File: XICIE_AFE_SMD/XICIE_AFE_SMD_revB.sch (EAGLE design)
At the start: 45 parts, among them IC1 LM324D, IC2 CY8C4245T, IC3 AAT1217, J1 22-27-2021-02, Q1 MOSFET-NCHANNELBSS123LT1G, Q2 MOSFET-NCHANNELBSS123LT1G, Q3 MOSFET-NCHANNELBSS123LT1G

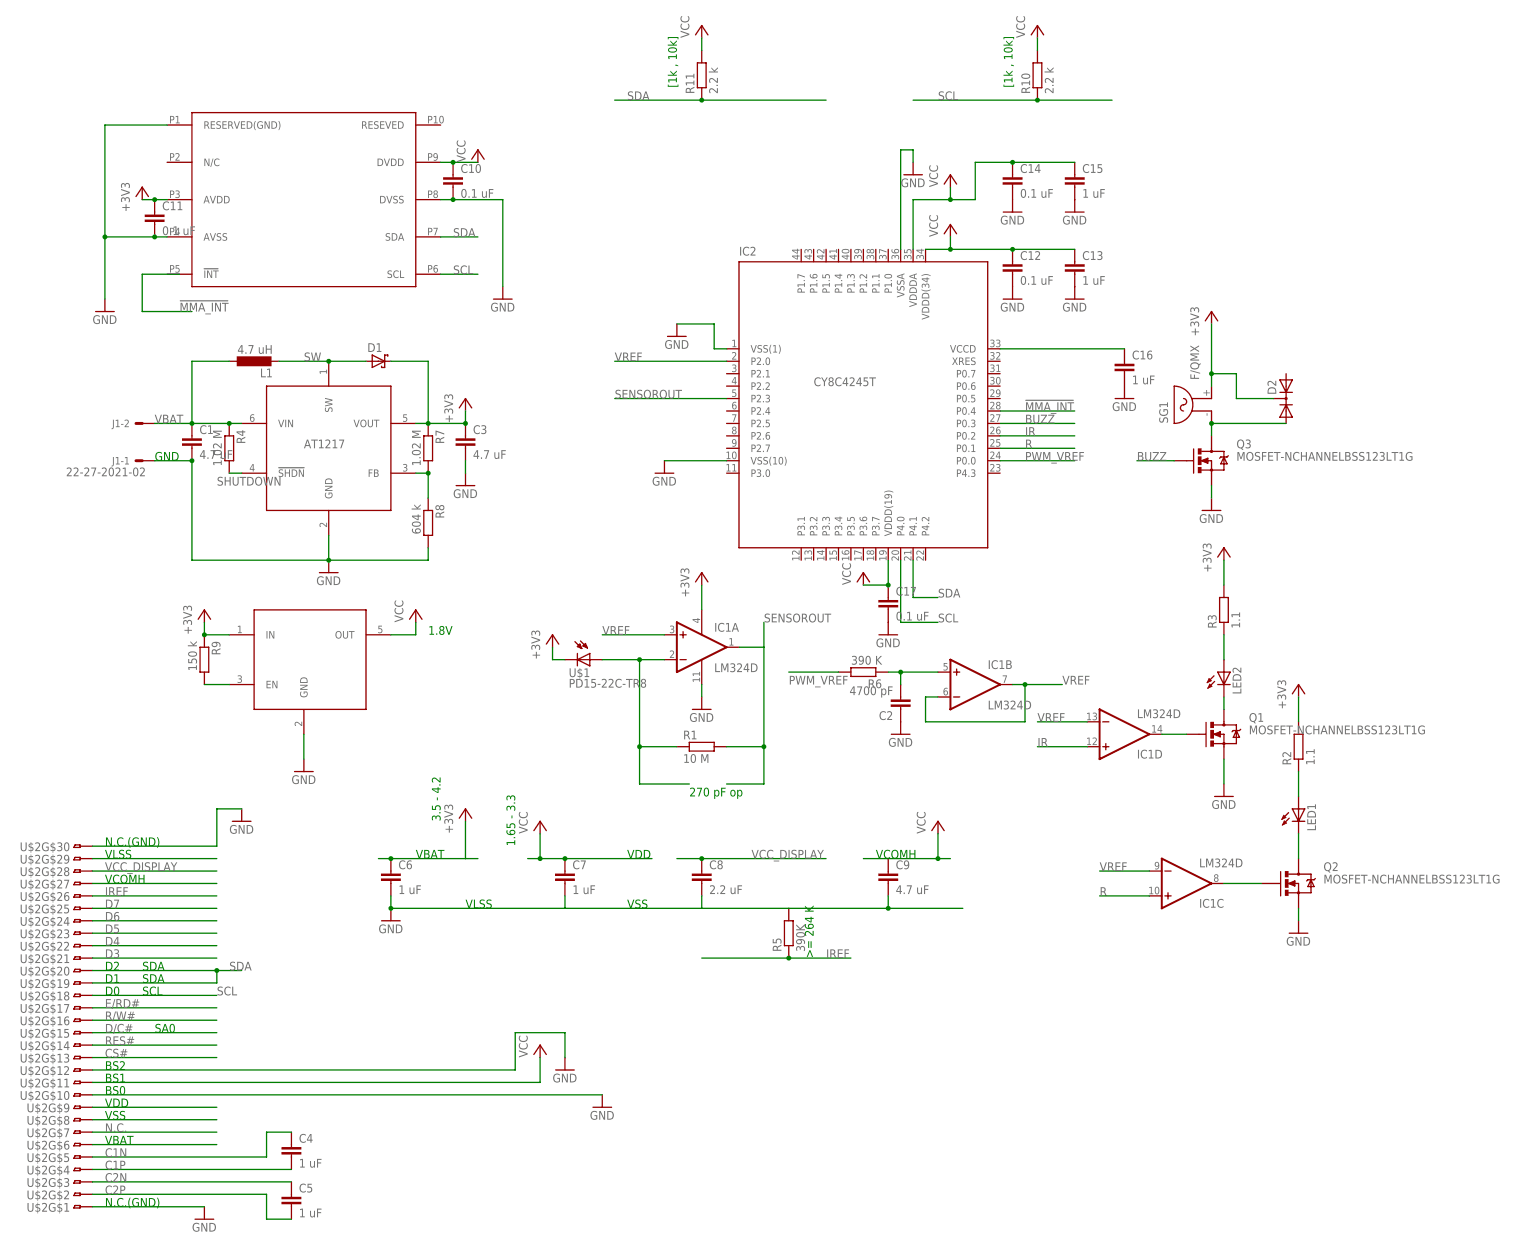
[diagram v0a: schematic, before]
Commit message: Finished rev B of XICIE_AFE_SMD
Many things added, like button, buzzer, RGB
led. Placing improved manually. Still missing
connection to program PSoC4.
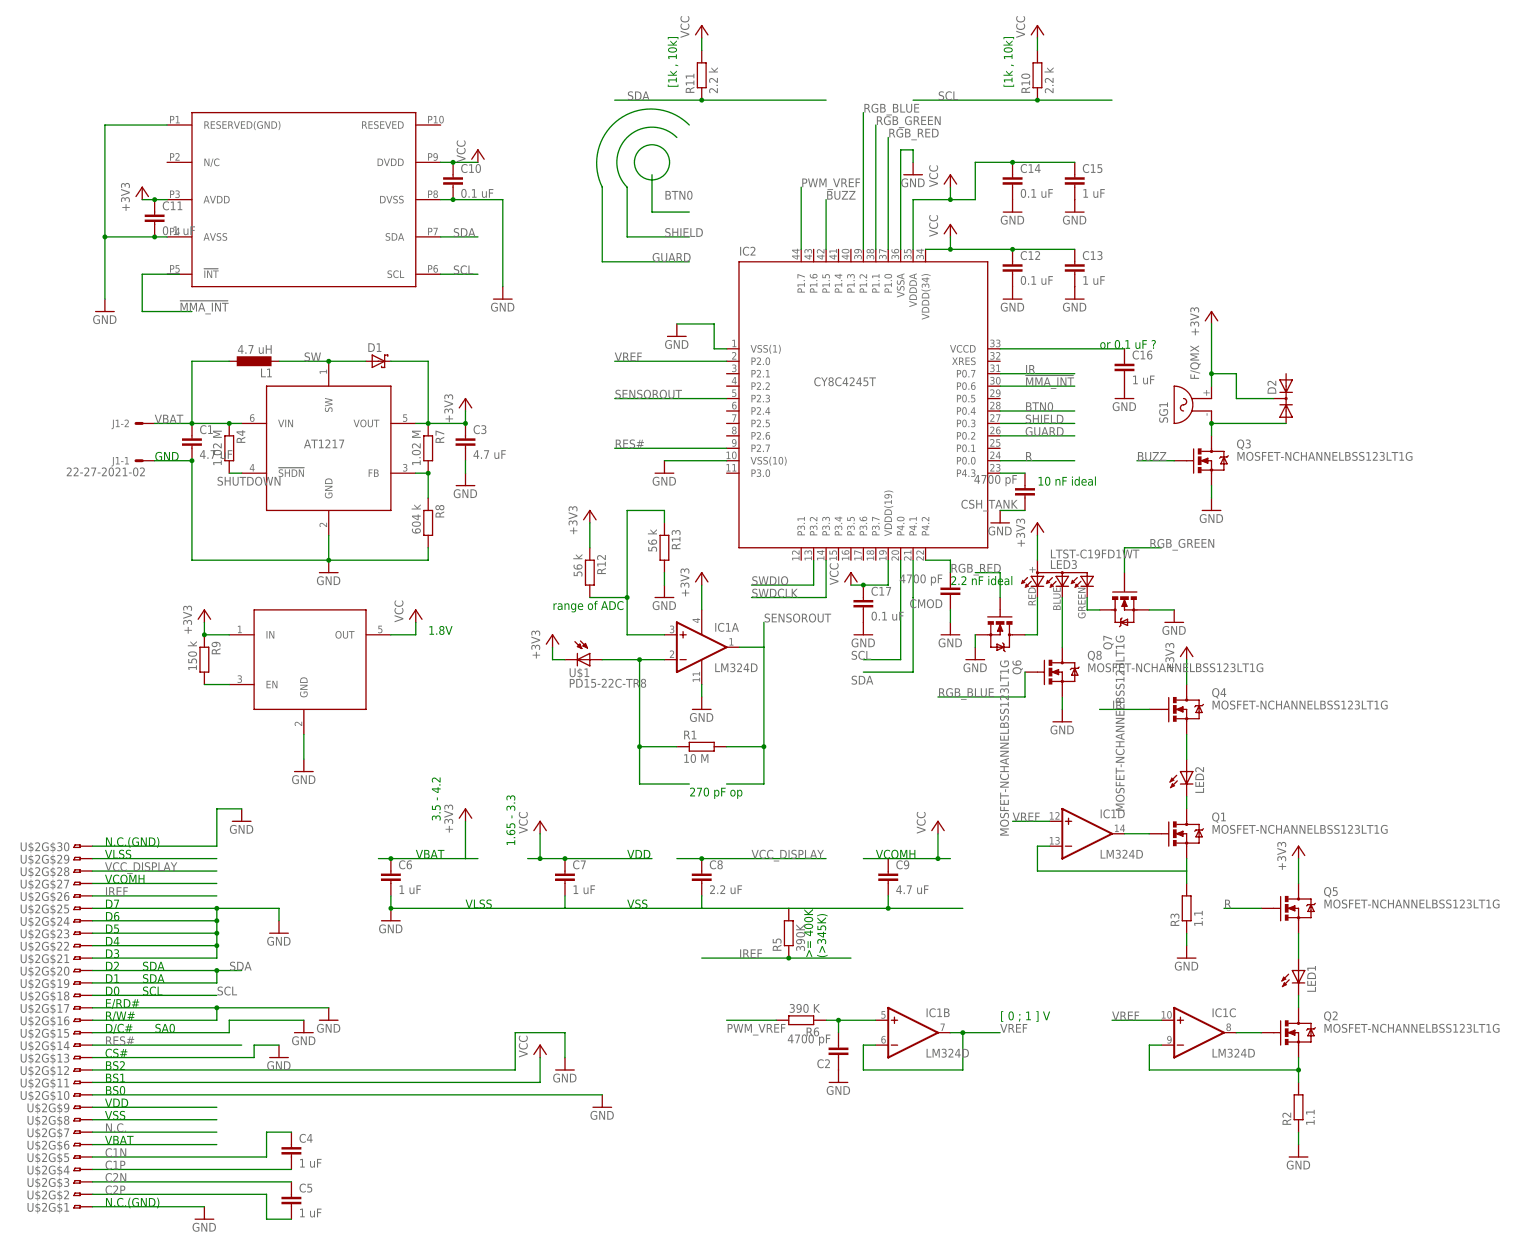
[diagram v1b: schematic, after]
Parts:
- added CMOD, CSH_TANK: 4700 pF, rcl:C-EUC0402
- added LED3: LTST-C19FD1WT, juliano:LTST-C19FD1WT
- added Q4, Q5, Q6, Q7, Q8: MOSFET-NCHANNELBSS123LT1G, SparkFun-DiscreteSemi:MOSFET-NCHANNELBSS123LT1G
- added R12, R13: 56 k, rcl:R-EU_R0603
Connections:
- removed net CS#: U$2G$13.1
- removed net D/C#: U$2G$15.1
- removed net D3: U$2G$21.1
- removed net D4: U$2G$22.1
- removed net D5: U$2G$23.1
- removed net D6: U$2G$24.1
- removed net D7: U$2G$25.1
- removed net E/RD#: U$2G$17.1
- removed net N$7 (its old number): LED1.A, R2.1
- removed net R/W#: U$2G$16.1
- new net BTN0: IC2.P0.4
- new net GUARD: IC2.P0.2
- new net N$15: IC1A.+IN, R12.2, R13.1
- new net N$16: LED1.A, Q5.S
- new net N$17: LED3.CRED, Q6.D
- new net N$18: LED3.CBLUE, Q8.D
- new net N$20: LED3.CGREEN, Q7.D
- new net N$21: CMOD.2, IC2.P4.2
- new net N$22: CSH_TANK.2, IC2.P4.3
- new net N$3: IC1C.-IN, Q2.S, R2.2
- new net N$4: LED2.A, Q4.S
- new net RGB_BLUE: IC2.P1.2, Q8.G
- new net RGB_GREEN: IC2.P1.1, Q7.G
- new net RGB_RED: IC2.P1.0, Q6.G
- new net SHIELD: IC2.P0.3
- new net SWDCLK: IC2.P3.3
- new net SWDIO: IC2.P3.2
- net !MMA_INT: now also IC2.P0.6; no longer IC2.P0.4
- net +3V3: now also LED3.A, Q4.D, Q5.D, R12.1; no longer R2.2, R3.2
- net BUZZ: now also IC2.P1.5; no longer IC2.P0.3
- net GND: now also CMOD.1, CSH_TANK.1, Q6.S, Q7.S, Q8.S, R13.2, R2.1, R3.1, U$2G$13.1, U$2G$15.1, U$2G$16.1, U$2G$17.1, U$2G$21.1, U$2G$22.1, U$2G$23.1, U$2G$24.1, U$2G$25.1; no longer Q1.S, Q2.S
- net IR: now also IC2.P0.7, Q4.G; no longer IC1D.+IN, IC2.P0.2
- net N$8: now also IC1D.-IN, Q1.S, R3.2; no longer LED2.A, R3.1
- net PWM_VREF: now also IC2.P1.7; no longer IC2.P0.0
- net R: now also IC2.P0.0, Q5.G; no longer IC1C.+IN, IC2.P0.1
- net RES#: now also IC2.P2.7
- net VREF: now also IC1C.+IN, IC1D.+IN; no longer IC1A.+IN, IC1C.-IN, IC1D.-IN
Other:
- note added: "10 nF ideal"
- note added: "2.2 nF ideal"
- note added: "CS#"
- note added: "D/C#"
- note added: "D3"
- note added: "D4"
- note added: "D5"
- note added: "D6"
- note added: "D7"
- note added: "E/RD#"
- note added: "R/W#"
- note added: "[ 0 ; 1 ] V"
- note added: "or 0.1 uF ?"
- note added: "range of ADC"
- moved on the sheet: C17, C2, IC1B, IC1C, IC1D, LED1, LED2, Q1, Q2, R2, R3, R6
